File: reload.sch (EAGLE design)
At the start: 17 parts, among them IC1 LM358, Q1 BTS117, U1 TL431

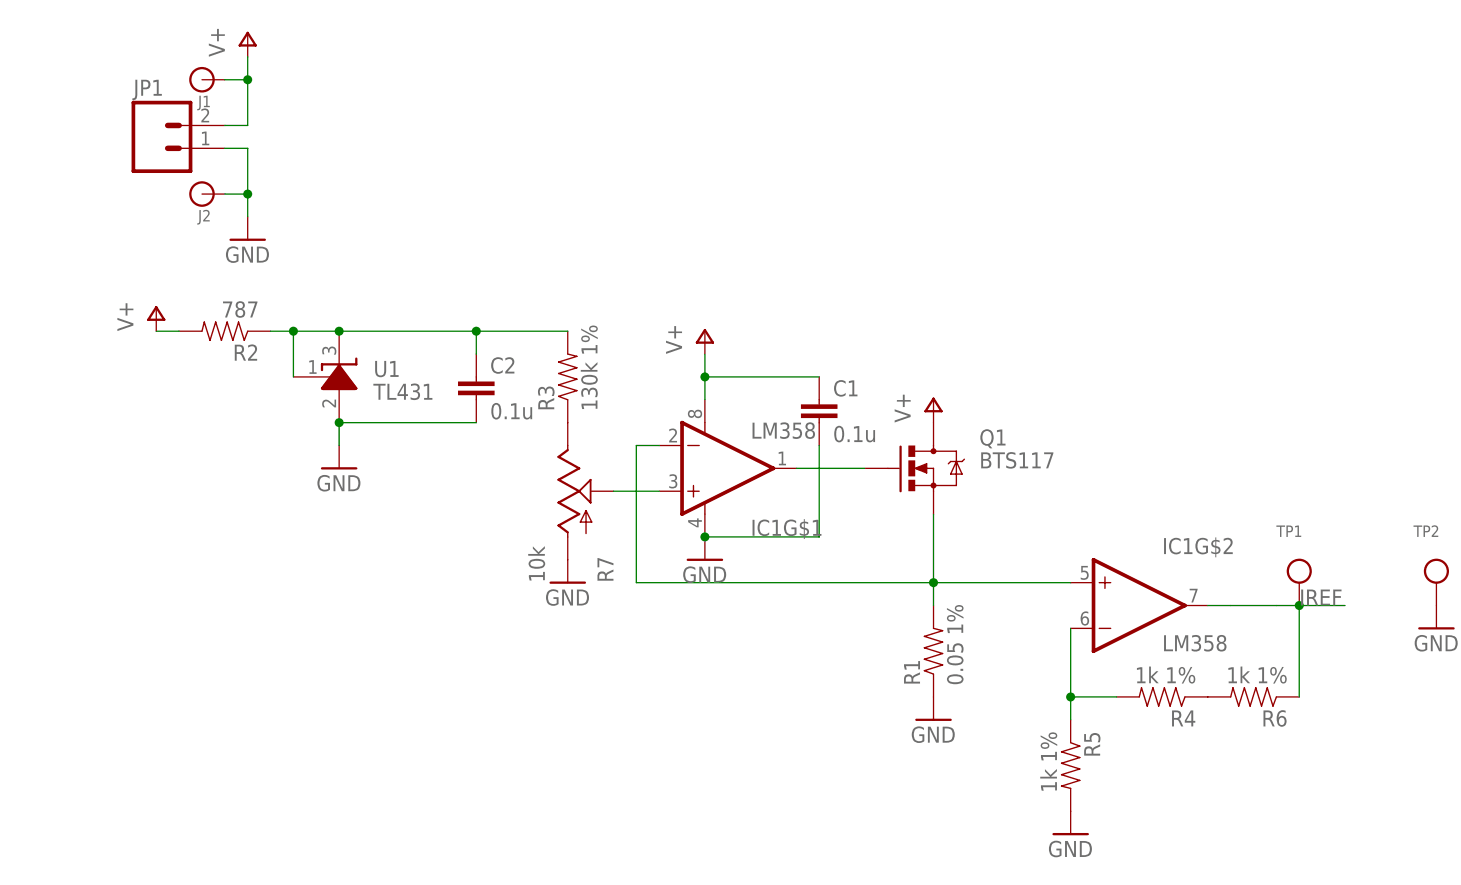
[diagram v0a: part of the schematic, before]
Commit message: Reworked to use a voltage regulator, added reverse protection diode, other improvements.
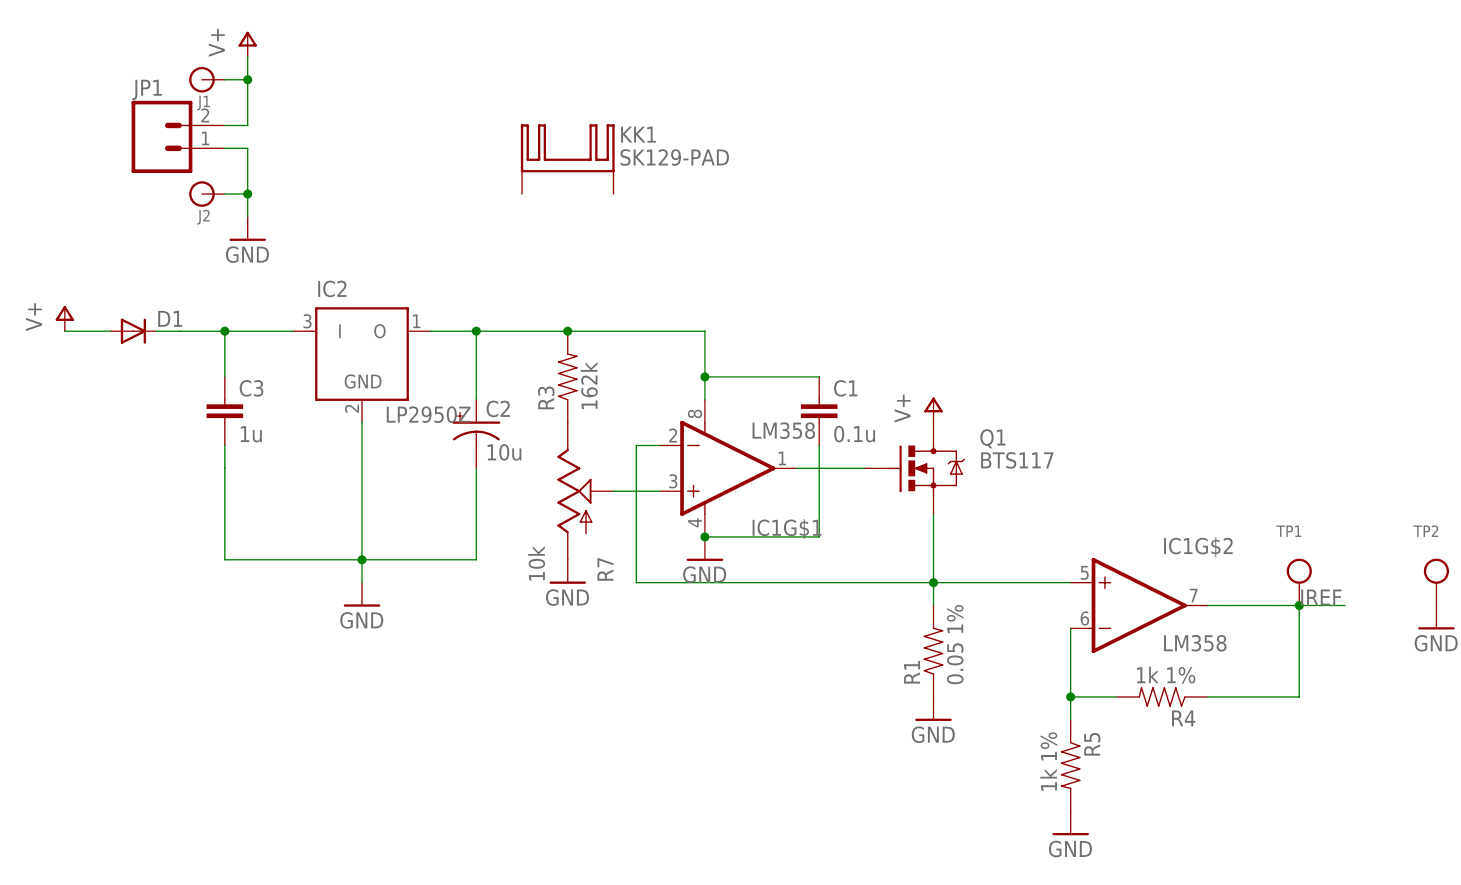
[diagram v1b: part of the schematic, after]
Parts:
- removed R2: 787, SparkFun-Passives:RESISTORAXIAL-0.3
- removed R6: 1k 1%, SparkFun-Passives:RESISTORAXIAL-0.3
- removed U1: TL431, GuShH:TL431
- added C3: 1u, SparkFun-Passives:CAPPTH1
- added D1: (no value), SparkFun-DiscreteSemi:DIODE1N4148
- added IC2: LP2950Z, linear:LP2950Z
- added KK1: SK129-PAD, nickparts:SK129-PAD
- C2: value 0.1u -> 10u; device SparkFun-Passives:CAPPTH -> SparkFun-Passives:CAP_POLPTH2
- R3: value 130k 1% -> 162k
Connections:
- removed net N$5: C2.1, R2.1, R3.2, U1.C, U1.REF
- removed net N$7: R4.1, R6.2
- new net 3V: C1.1, C2.+, IC1G$1.V+, IC2.O, R3.2
- new net N$8: C3.1, D1.C, IC2.I
- net GND: now also C2.-, C3.2, IC2.GND; no longer C2.2, U1.A
- net IREF: now also R4.1; no longer R6.1
- net V+: now also D1.A; no longer C1.1, IC1G$1.V+, R2.2
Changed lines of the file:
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@@
 <part name="P+1" library="supply1" deviceset="V+" device=""/>
 <part name="GND1" library="supply1" deviceset="GND" device=""/>
-<part name="P+2" library="supply1" deviceset="V+" device=""/>
 <part name="GND2" library="supply1" deviceset="GND" device=""/>
 <part name="R7" library="SparkFun-Electromechanical" deviceset="POT" device="" value="10k"/>
 <part name="GND3" library="supply1" deviceset="GND" device=""/>
-<part name="R3" library="SparkFun-Passives" deviceset="RESISTOR" device="AXIAL-0.3" value="130k 1%"/>
-<part name="U1" library="GuShH" deviceset="TL431" device=""/>
+<part name="R3" library="SparkFun-Passives" deviceset="RESISTOR" device="AXIAL-0.3" value="162k"/>
 <part name="GND4" library="supply1" deviceset="GND" device=""/>
 <part name="P+3" library="supply1" deviceset="V+" device=""/>
-<part name="R2" library="SparkFun-Passives" deviceset="RESISTOR" device="AXIAL-0.3" value="787"/>
 <part name="C1" library="SparkFun-Passives" deviceset="CAP" device="PTH" value="0.1u"/>
-<part name="C2" library="SparkFun-Passives" deviceset="CAP" device="PTH" value="0.1u"/>
 <part name="R5" library="SparkFun-Passives" deviceset="RESISTOR" device="AXIAL-0.3" value="1k 1%"/>
 <part name="GND5" library="supply1" deviceset="GND" device=""/>
-<part name="R6" library="SparkFun-Passives" deviceset="RESISTOR" device="AXIAL-0.3" value="1k 1%"/>
 <part name="TP1" library="microbuilder" deviceset="TESTPOINT" device="0.1&quot;"/>
 <part name="TP2" library="microbuilder" deviceset="TESTPOINT" device="0.1&quot;">
@@
 <part name="P+4" library="supply1" deviceset="V+" device=""/>
 <part name="GND7" library="supply1" deviceset="GND" device=""/>
+<part name="C2" library="SparkFun-Passives" deviceset="CAP_POL" device="PTH2" value="10u"/>
+<part name="D1" library="SparkFun-DiscreteSemi" deviceset="DIODE" device="1N4148"/>
+<part name="IC2" library="linear" deviceset="LP2950" device="Z"/>
+<part name="C3" library="SparkFun-Passives" deviceset="CAP" device="PTH1" value="1u"/>
+<part name="KK1" library="nickparts" deviceset="SK129-PAD" device=""/>
 </parts>
 <sheets>
@@
 <instance part="P+1" gate="1" x="58.42" y="43.18"/>
 <instance part="GND1" gate="1" x="58.42" y="7.62"/>
-<instance part="P+2" gate="1" x="33.02" y="50.8"/>
 <instance part="GND2" gate="1" x="33.02" y="25.4"/>
 <instance part="R7" gate="G$1" x="17.78" y="33.02"/>
 <instance part="GND3" gate="1" x="17.78" y="22.86"/>
 <instance part="R3" gate="G$1" x="17.78" y="45.72" rot="R90"/>
-<instance part="U1" gate="G$1" x="-7.62" y="45.72"/>
-<instance part="GND4" gate="1" x="-7.62" y="35.56"/>
-<instance part="P+3" gate="1" x="-27.94" y="53.34"/>
-<instance part="R2" gate="G$1" x="-20.32" y="50.8" rot="R180"/>
+<instance part="GND4" gate="1" x="-5.08" y="20.32"/>
+<instance part="P+3" gate="1" x="-38.1" y="53.34"/>
 <instance part="C1" gate="G$1" x="45.72" y="40.64"/>
-<instance part="C2" gate="G$1" x="7.62" y="43.18"/>
 <instance part="IC1" gate="G$2" x="81.28" y="20.32"/>
 <instance part="R5" gate="G$1" x="73.66" y="2.54" rot="R270"/>
 <instance part="GND5" gate="1" x="73.66" y="-5.08"/>
-<instance part="R6" gate="G$1" x="93.98" y="10.16" rot="R180"/>
 <instance part="TP1" gate="G$1" x="99.06" y="20.32"/>
 <instance part="TP2" gate="G$1" x="114.3" y="20.32"/>
@@
 <instance part="P+4" gate="1" x="-17.78" y="83.82"/>
 <instance part="GND7" gate="1" x="-17.78" y="60.96"/>
+<instance part="C2" gate="G$1" x="7.62" y="40.64"/>
+<instance part="D1" gate="G$1" x="-30.48" y="50.8"/>
+<instance part="IC2" gate="G$1" x="-5.08" y="48.26"/>
+<instance part="C3" gate="G$1" x="-20.32" y="40.64"/>
+<instance part="KK1" gate="G$1" x="17.78" y="68.58"/>
 </instances>
 <busses>
@@
 <pinref part="Q1" gate="G$1" pin="D"/>
 <pinref part="P+1" gate="1" pin="V+"/>
-</segment>
-<segment>
-<pinref part="IC1" gate="G$1" pin="V+"/>
-<pinref part="P+2" gate="1" pin="V+"/>
-<wire x1="33.02" y1="48.26" x2="33.02" y2="45.72" width="0.1524" layer="91"/>
-<pinref part="C1" gate="G$1" pin="1"/>
-<wire x1="33.02" y1="45.72" x2="33.02" y2="43.18" width="0.1524" layer="91"/>
-<wire x1="45.72" y1="45.72" x2="33.02" y2="45.72" width="0.1524" layer="91"/>
-<junction x="33.02" y="45.72"/>
-</segment>
-<segment>
-<pinref part="P+3" gate="1" pin="V+"/>
-<pinref part="R2" gate="G$1" pin="2"/>
-<wire x1="-27.94" y1="50.8" x2="-25.4" y2="50.8" width="0.1524" layer="91"/>
 </segment>
 <segment>
@@
 <wire x1="-20.32" y1="78.74" x2="-17.78" y2="78.74" width="0.1524" layer="91"/>
 <junction x="-17.78" y="78.74"/>
+</segment>
+<segment>
+<pinref part="P+3" gate="1" pin="V+"/>
+<pinref part="D1" gate="G$1" pin="A"/>
+<wire x1="-38.1" y1="50.8" x2="-33.02" y2="50.8" width="0.1524" layer="91"/>
 </segment>
 </net>
@@
 </segment>
 <segment>
-<pinref part="U1" gate="G$1" pin="A"/>
 <pinref part="GND4" gate="1" pin="GND"/>
-<wire x1="-7.62" y1="38.1" x2="-7.62" y2="40.64" width="0.1524" layer="91"/>
-<pinref part="C2" gate="G$1" pin="2"/>
-<wire x1="-7.62" y1="40.64" x2="7.62" y2="40.64" width="0.1524" layer="91"/>
-<junction x="-7.62" y="40.64"/>
+<wire x1="-5.08" y1="22.86" x2="-5.08" y2="25.4" width="0.1524" layer="91"/>
+<pinref part="C2" gate="G$1" pin="-"/>
+<wire x1="7.62" y1="35.56" x2="7.62" y2="25.4" width="0.1524" layer="91"/>
+<wire x1="7.62" y1="25.4" x2="-5.08" y2="25.4" width="0.1524" layer="91"/>
+<wire x1="-5.08" y1="25.4" x2="-20.32" y2="25.4" width="0.1524" layer="91"/>
+<wire x1="-20.32" y1="25.4" x2="-20.32" y2="35.56" width="0.1524" layer="91"/>
+<junction x="-5.08" y="25.4"/>
+<pinref part="C3" gate="G$1" pin="2"/>
+<wire x1="-20.32" y1="35.56" x2="-20.32" y2="38.1" width="0.1524" layer="91"/>
+<pinref part="IC2" gate="G$1" pin="GND"/>
+<wire x1="-5.08" y1="40.64" x2="-5.08" y2="25.4" width="0.1524" layer="91"/>
 </segment>
 <segment>
@@
 </segment>
 </net>
-<net name="N$5" class="0">
-<segment>
-<pinref part="U1" gate="G$1" pin="C"/>
-<pinref part="R2" gate="G$1" pin="1"/>
-<wire x1="-15.24" y1="50.8" x2="-12.7" y2="50.8" width="0.1524" layer="91"/>
-<pinref part="U1" gate="G$1" pin="REF"/>
-<wire x1="-12.7" y1="50.8" x2="-7.62" y2="50.8" width="0.1524" layer="91"/>
-<wire x1="-12.7" y1="45.72" x2="-12.7" y2="50.8" width="0.1524" layer="91"/>
-<junction x="-12.7" y="50.8"/>
-<pinref part="R3" gate="G$1" pin="2"/>
-<wire x1="-7.62" y1="50.8" x2="7.62" y2="50.8" width="0.1524" layer="91"/>
-<junction x="-7.62" y="50.8"/>
-<pinref part="C2" gate="G$1" pin="1"/>
-<wire x1="7.62" y1="50.8" x2="17.78" y2="50.8" width="0.1524" layer="91"/>
-<wire x1="7.62" y1="48.26" x2="7.62" y2="50.8" width="0.1524" layer="91"/>
-<junction x="7.62" y="50.8"/>
-</segment>
-</net>
 <net name="N$6" class="0">
 <segment>
@@
 <wire x1="88.9" y1="20.32" x2="91.44" y2="20.32" width="0.1524" layer="91"/>
 <wire x1="91.44" y1="20.32" x2="96.52" y2="20.32" width="0.1524" layer="91"/>
-<pinref part="R6" gate="G$1" pin="1"/>
 <wire x1="99.06" y1="10.16" x2="99.06" y2="20.32" width="0.1524" layer="91"/>
 <wire x1="99.06" y1="20.32" x2="96.52" y2="20.32" width="0.1524" layer="91"/>
@@
 <label x="99.06" y="20.32" size="1.778" layer="95"/>
 <pinref part="TP1" gate="G$1" pin="P$1"/>
-</segment>
-</net>
-<net name="N$7" class="0">
-<segment>
-<pinref part="R6" gate="G$1" pin="2"/>
 <pinref part="R4" gate="G$1" pin="1"/>
-</segment>
-</net>
+<wire x1="88.9" y1="10.16" x2="99.06" y2="10.16" width="0.1524" layer="91"/>
+</segment>
+</net>
+<net name="3V" class="0">
+<segment>
+<pinref part="R3" gate="G$1" pin="2"/>
+<wire x1="7.62" y1="50.8" x2="17.78" y2="50.8" width="0.1524" layer="91"/>
+<wire x1="7.62" y1="43.18" x2="7.62" y2="50.8" width="0.1524" layer="91"/>
+<pinref part="C2" gate="G$1" pin="+"/>
+<pinref part="IC1" gate="G$1" pin="V+"/>
+<pinref part="C1" gate="G$1" pin="1"/>
+<wire x1="33.02" y1="45.72" x2="33.02" y2="43.18" width="0.1524" layer="91"/>
+<wire x1="45.72" y1="45.72" x2="33.02" y2="45.72" width="0.1524" layer="91"/>
+<wire x1="17.78" y1="50.8" x2="33.02" y2="50.8" width="0.1524" layer="91"/>
+<wire x1="33.02" y1="50.8" x2="33.02" y2="45.72" width="0.1524" layer="91"/>
+<junction x="17.78" y="50.8"/>
+<junction x="33.02" y="45.72"/>
+<pinref part="IC2" gate="G$1" pin="O"/>
+<wire x1="2.54" y1="50.8" x2="7.62" y2="50.8" width="0.1524" layer="91"/>
+<junction x="7.62" y="50.8"/>
+</segment>
+</net>
+<net name="N$8" class="0">
+<segment>
+<pinref part="D1" gate="G$1" pin="C"/>
+<wire x1="-27.94" y1="50.8" x2="-25.4" y2="50.8" width="0.1524" layer="91"/>
+<pinref part="IC2" gate="G$1" pin="I"/>
+<wire x1="-25.4" y1="50.8" x2="-20.32" y2="50.8" width="0.1524" layer="91"/>
+<pinref part="C3" gate="G$1" pin="1"/>
+<wire x1="-20.32" y1="50.8" x2="-12.7" y2="50.8" width="0.1524" layer="91"/>
+<wire x1="-20.32" y1="45.72" x2="-20.32" y2="50.8" width="0.1524" layer="91"/>
+<junction x="-20.32" y="50.8"/>
+</segment>
+</net>

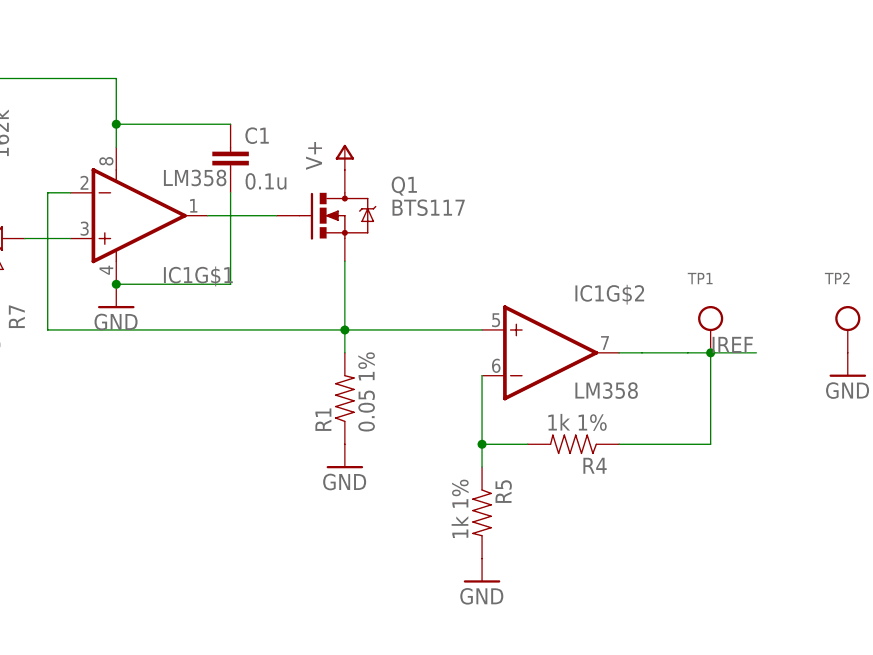
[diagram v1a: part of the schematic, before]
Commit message: Added trimpot on back side of board; minor other layout tweaks.
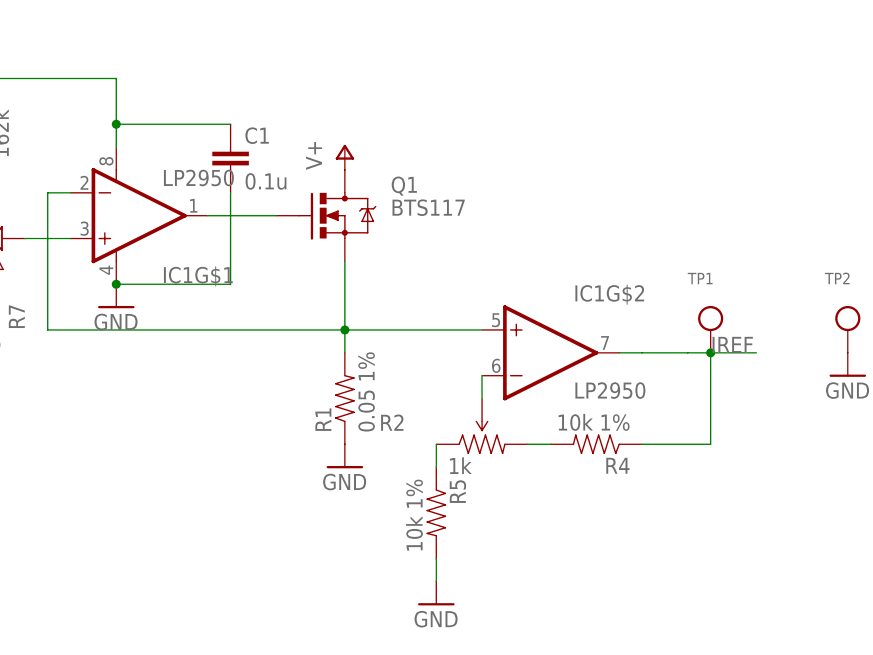
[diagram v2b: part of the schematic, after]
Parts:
- added R2: 1k, nickparts:TRIMPOT3MM-2
- IC1: value LM358 -> LP2950
- R4, R5: value 1k 1% -> 10k 1%
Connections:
- new net N$5: IC1G$2.-IN, R2.WIPER
- new net N$7: R2.CW, R4.2
- net N$6: now also R2.CCW; no longer IC1G$2.-IN, R4.2
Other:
- moved on the sheet: R4, R5
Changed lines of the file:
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@@
 </classes>
 <parts>
-<part name="IC1" library="SparkFun-AnalogIC" deviceset="LM358" device=""/>
+<part name="IC1" library="SparkFun-AnalogIC" deviceset="LM358" device="" value="LP2950"/>
 <part name="R1" library="SparkFun-Passives" deviceset="RESISTOR" device="PTH-1W" value="0.05 1%"/>
 <part name="Q1" library="SparkFun-DiscreteSemi" deviceset="MOSFET-NCHANNEL" device="PTH2" value="BTS117"/>
@@
 <part name="P+3" library="supply1" deviceset="V+" device=""/>
 <part name="C1" library="SparkFun-Passives" deviceset="CAP" device="PTH" value="0.1u"/>
-<part name="R5" library="SparkFun-Passives" deviceset="RESISTOR" device="AXIAL-0.3" value="1k 1%"/>
+<part name="R5" library="SparkFun-Passives" deviceset="RESISTOR" device="AXIAL-0.3" value="10k 1%"/>
 <part name="GND5" library="supply1" deviceset="GND" device=""/>
 <part name="TP1" library="microbuilder" deviceset="TESTPOINT" device="0.1&quot;"/>
@@
 </part>
 <part name="GND6" library="supply1" deviceset="GND" device=""/>
-<part name="R4" library="SparkFun-Passives" deviceset="RESISTOR" device="AXIAL-0.3" value="1k 1%"/>
+<part name="R4" library="SparkFun-Passives" deviceset="RESISTOR" device="AXIAL-0.3" value="10k 1%"/>
 <part name="P+4" library="supply1" deviceset="V+" device=""/>
 <part name="GND7" library="supply1" deviceset="GND" device=""/>
@@
 <part name="C3" library="SparkFun-Passives" deviceset="CAP" device="PTH1" value="1u"/>
 <part name="KK1" library="nickparts" deviceset="SK129-PAD" device=""/>
+<part name="R2" library="nickparts" deviceset="TRIMPOT" device="3MM-2" value="1k"/>
 </parts>
 <sheets>
@@
 <instance part="C1" gate="G$1" x="45.72" y="40.64"/>
 <instance part="IC1" gate="G$2" x="81.28" y="20.32"/>
-<instance part="R5" gate="G$1" x="73.66" y="2.54" rot="R270"/>
-<instance part="GND5" gate="1" x="73.66" y="-5.08"/>
+<instance part="R5" gate="G$1" x="68.58" y="2.54" rot="R270"/>
+<instance part="GND5" gate="1" x="68.58" y="-7.62"/>
 <instance part="TP1" gate="G$1" x="99.06" y="20.32"/>
 <instance part="TP2" gate="G$1" x="114.3" y="20.32"/>
 <instance part="GND6" gate="1" x="114.3" y="17.78"/>
-<instance part="R4" gate="G$1" x="83.82" y="10.16" rot="R180"/>
+<instance part="R4" gate="G$1" x="86.36" y="10.16" rot="R180"/>
 <instance part="P+4" gate="1" x="-17.78" y="83.82"/>
 <instance part="GND7" gate="1" x="-17.78" y="60.96"/>
@@
 <instance part="C3" gate="G$1" x="-20.32" y="40.64"/>
 <instance part="KK1" gate="G$1" x="17.78" y="68.58"/>
+<instance part="R2" gate="R?" x="73.66" y="10.16"/>
 </instances>
 <busses>
@@
 <pinref part="R5" gate="G$1" pin="2"/>
 <pinref part="GND5" gate="1" pin="GND"/>
+<wire x1="68.58" y1="-2.54" x2="68.58" y2="-5.08" width="0.1524" layer="91"/>
 </segment>
 <segment>
@@
 <pinref part="IC1" gate="G$1" pin="+IN"/>
 <wire x1="22.86" y1="33.02" x2="27.94" y2="33.02" width="0.1524" layer="91"/>
-</segment>
-</net>
-<net name="N$6" class="0">
-<segment>
-<pinref part="IC1" gate="G$2" pin="-IN"/>
-<pinref part="R5" gate="G$1" pin="1"/>
-<wire x1="73.66" y1="17.78" x2="73.66" y2="10.16" width="0.1524" layer="91"/>
-<wire x1="73.66" y1="10.16" x2="73.66" y2="7.62" width="0.1524" layer="91"/>
-<wire x1="78.74" y1="10.16" x2="73.66" y2="10.16" width="0.1524" layer="91"/>
-<junction x="73.66" y="10.16"/>
-<pinref part="R4" gate="G$1" pin="2"/>
 </segment>
 </net>
@@
 <pinref part="TP1" gate="G$1" pin="P$1"/>
 <pinref part="R4" gate="G$1" pin="1"/>
-<wire x1="88.9" y1="10.16" x2="99.06" y2="10.16" width="0.1524" layer="91"/>
+<wire x1="91.44" y1="10.16" x2="99.06" y2="10.16" width="0.1524" layer="91"/>
 </segment>
 </net>
@@
 </segment>
 </net>
+<net name="N$7" class="0">
+<segment>
+<pinref part="R4" gate="G$1" pin="2"/>
+<wire x1="81.28" y1="10.16" x2="78.74" y2="10.16" width="0.1524" layer="91"/>
+<pinref part="R2" gate="R?" pin="CW"/>
+</segment>
+</net>
+<net name="N$5" class="0">
+<segment>
+<pinref part="IC1" gate="G$2" pin="-IN"/>
+<pinref part="R2" gate="R?" pin="WIPER"/>
+<wire x1="73.66" y1="17.78" x2="73.66" y2="15.24" width="0.1524" layer="91"/>
+</segment>
+</net>
+<net name="N$6" class="0">
+<segment>
+<pinref part="R5" gate="G$1" pin="1"/>
+<pinref part="R2" gate="R?" pin="CCW"/>
+<wire x1="68.58" y1="7.62" x2="68.58" y2="10.16" width="0.1524" layer="91"/>
+</segment>
+</net>
